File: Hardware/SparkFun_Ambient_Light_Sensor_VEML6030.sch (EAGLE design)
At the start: 26 parts, among them U1 VEML6030

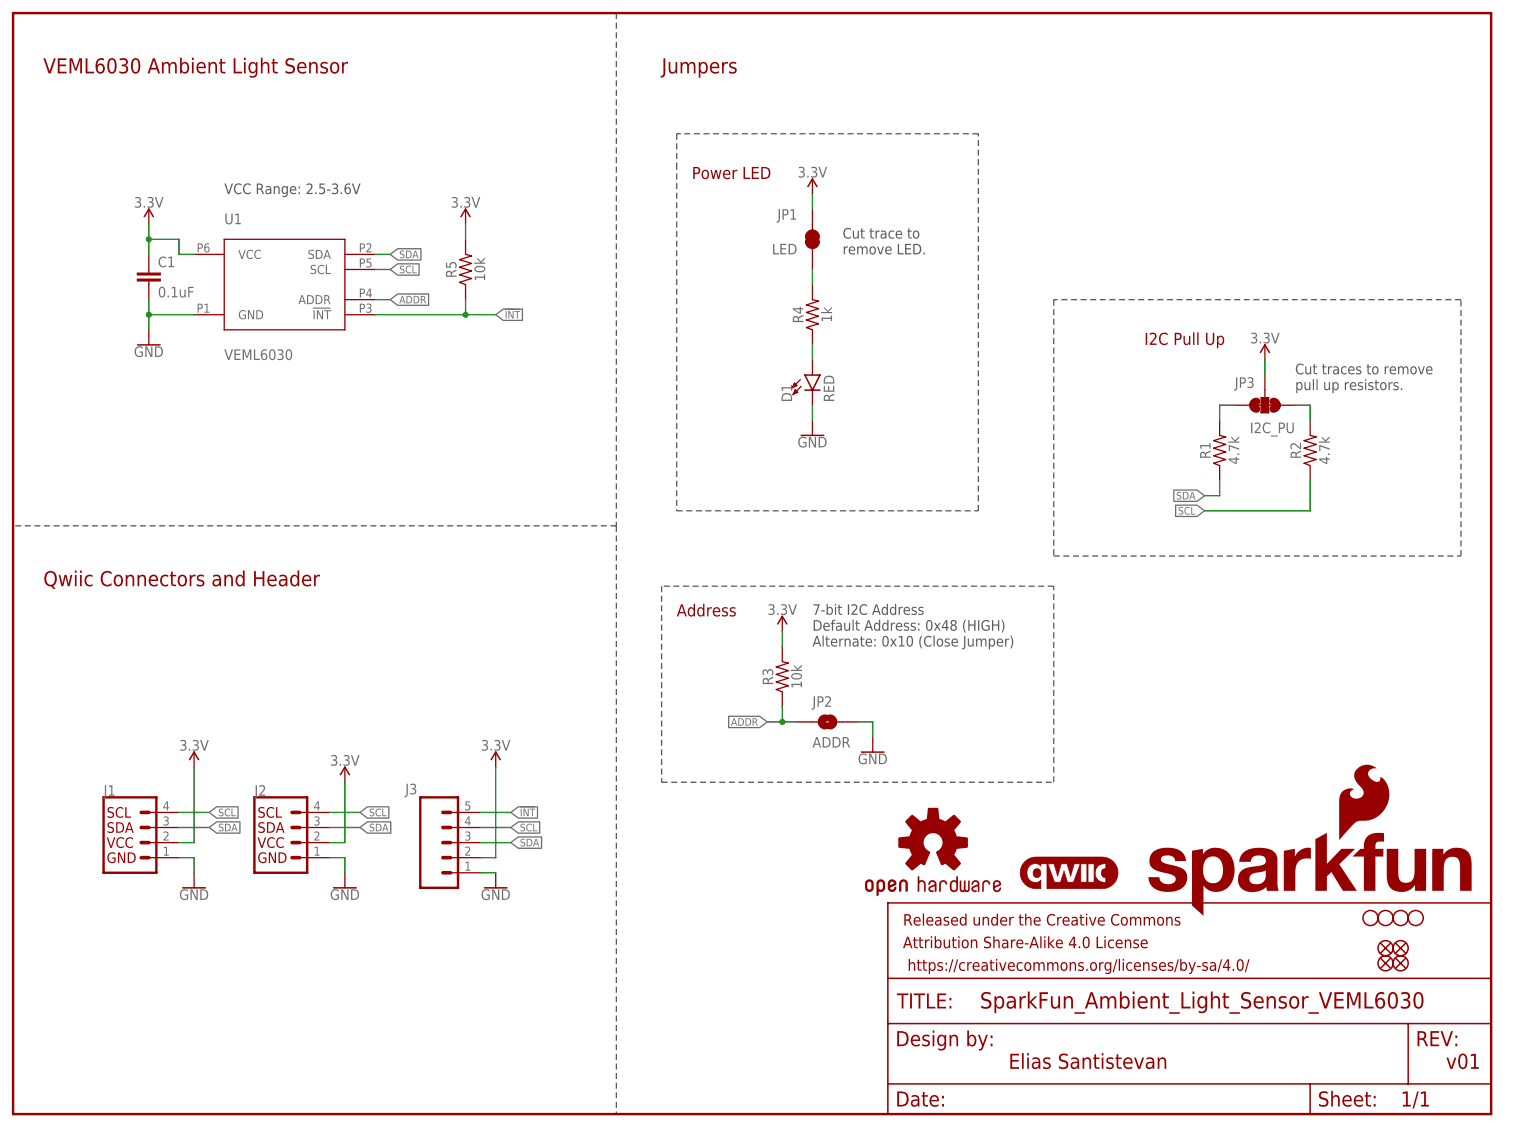
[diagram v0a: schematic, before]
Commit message: Routes 3.3V line on underside and data lines on the topside...
* Adds silk on the underside for address selection
* Adds power silk to LED
* moves resistor to top side
* Fixes GND net on 5 pin header
* Changes version to v10
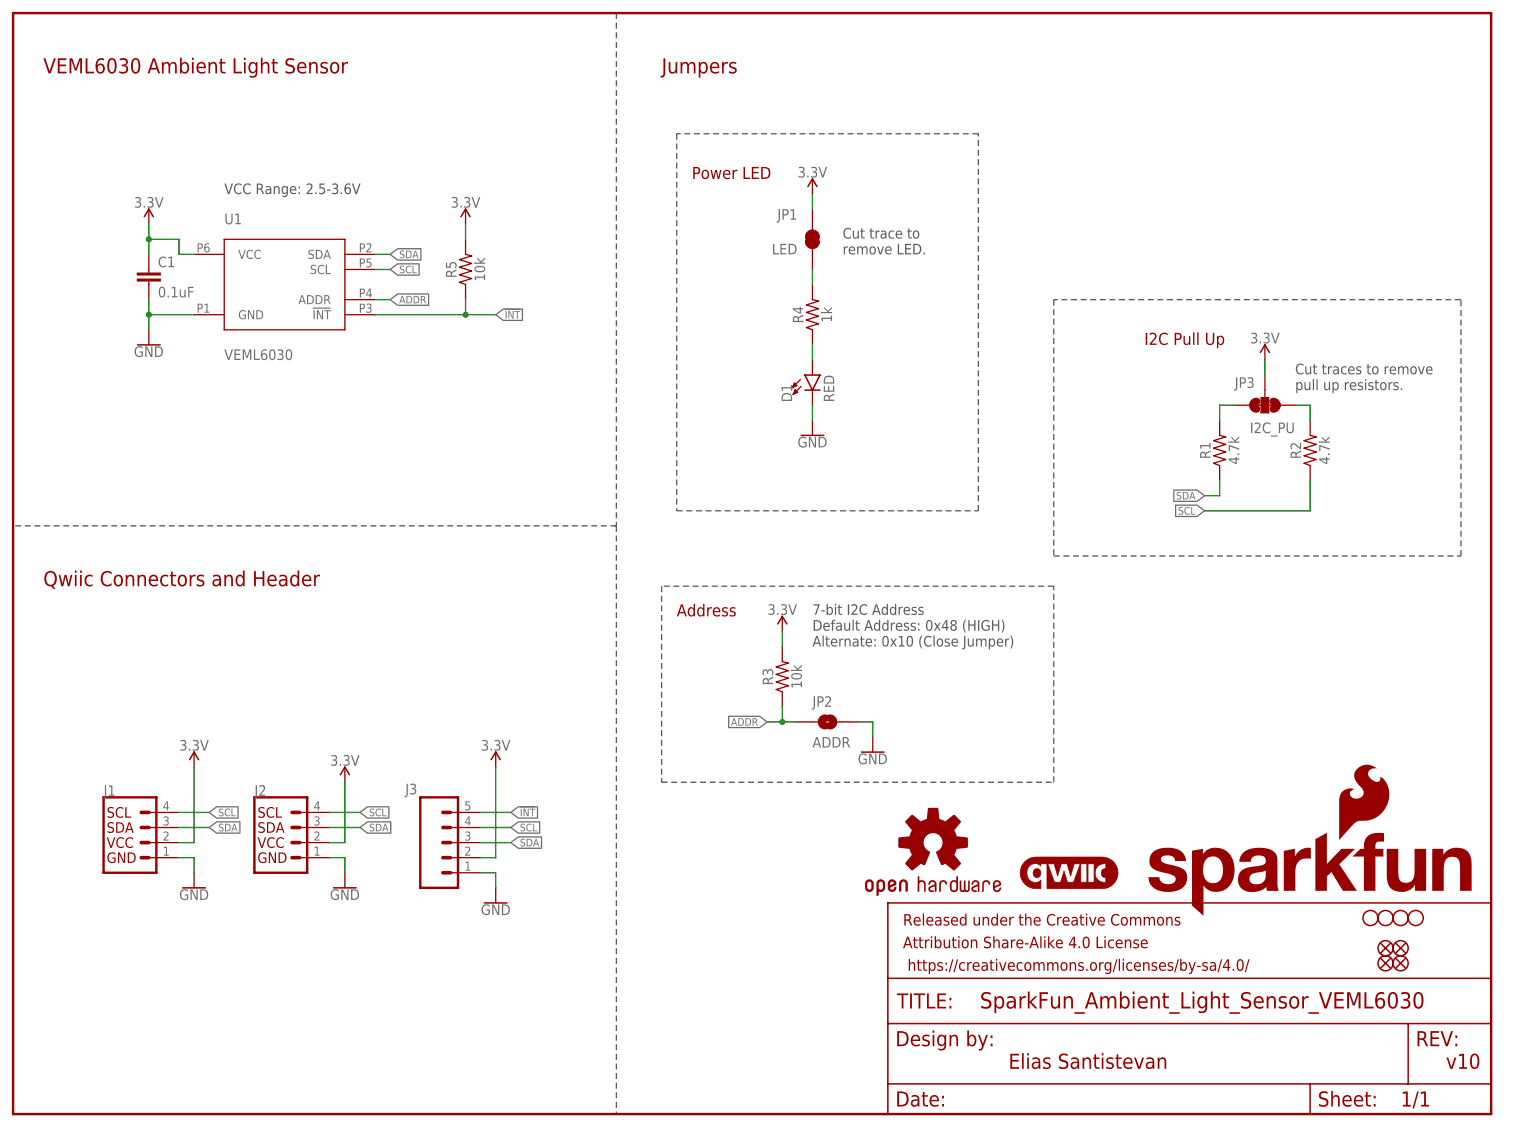
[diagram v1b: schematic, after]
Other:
- note added: "v10"
- note removed: "v01"
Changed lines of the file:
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@@
 <sheet>
 <plain>
-<text x="241.3" y="7.62" size="2.54" layer="94" font="vector">v01</text>
+<text x="241.3" y="7.62" size="2.54" layer="94" font="vector">v10</text>
 <text x="167.64" y="7.62" size="2.54" layer="94" font="vector">Elias Santistevan</text>
 <wire x1="101.6" y1="185.42" x2="101.6" y2="99.06" width="0.1524" layer="97" style="shortdash"/>
@@
 <text x="215.9" y="121.92" size="1.778" layer="97" font="vector">Cut traces to remove
 pull up resistors.</text>
-<wire x1="111.76" y1="160.02" x2="111.76" y2="101.6" width="0.2032" layer="97" style="shortdash"/>
+<wire x1="111.76" y1="165.1" x2="111.76" y2="101.6" width="0.2032" layer="97" style="shortdash"/>
 <wire x1="111.76" y1="101.6" x2="162.56" y2="101.6" width="0.2032" layer="97" style="shortdash"/>
 <wire x1="162.56" y1="101.6" x2="162.56" y2="165.1" width="0.2032" layer="97" style="shortdash"/>
 <wire x1="162.56" y1="165.1" x2="111.76" y2="165.1" width="0.2032" layer="97" style="shortdash"/>
-<wire x1="111.76" y1="165.1" x2="111.76" y2="160.02" width="0.2032" layer="97" style="shortdash"/>
 <wire x1="109.22" y1="88.9" x2="109.22" y2="55.88" width="0.2032" layer="97" style="shortdash"/>
 <wire x1="109.22" y1="55.88" x2="175.26" y2="55.88" width="0.2032" layer="97" style="shortdash"/>
@@
 <attribute name="VALUE" x="55.88" y="37.846" size="1.778" layer="96" font="vector" align="top-center"/>
 </instance>
-<instance part="GND4" gate="1" x="81.28" y="38.1" smashed="yes">
-<attribute name="VALUE" x="81.28" y="37.846" size="1.778" layer="96" font="vector" align="top-center"/>
+<instance part="GND4" gate="1" x="81.28" y="35.56" smashed="yes">
+<attribute name="VALUE" x="81.28" y="35.306" size="1.778" layer="96" font="vector" align="top-center"/>
 </instance>
 <instance part="R4" gate="G$1" x="134.62" y="134.62" smashed="yes" rot="R90">
@@
 <pinref part="GND4" gate="1" pin="GND"/>
 <wire x1="78.74" y1="40.64" x2="81.28" y2="40.64" width="0.1524" layer="91"/>
-</segment>
-<segment>
+<wire x1="81.28" y1="40.64" x2="81.28" y2="38.1" width="0.1524" layer="91"/>
+</segment>
+<segment>
